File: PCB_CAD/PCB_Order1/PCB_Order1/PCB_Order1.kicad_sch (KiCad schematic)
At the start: 2 parts, among them IC1 TC58BVG1S3HTA00, U1 STM32H7A3ZITx

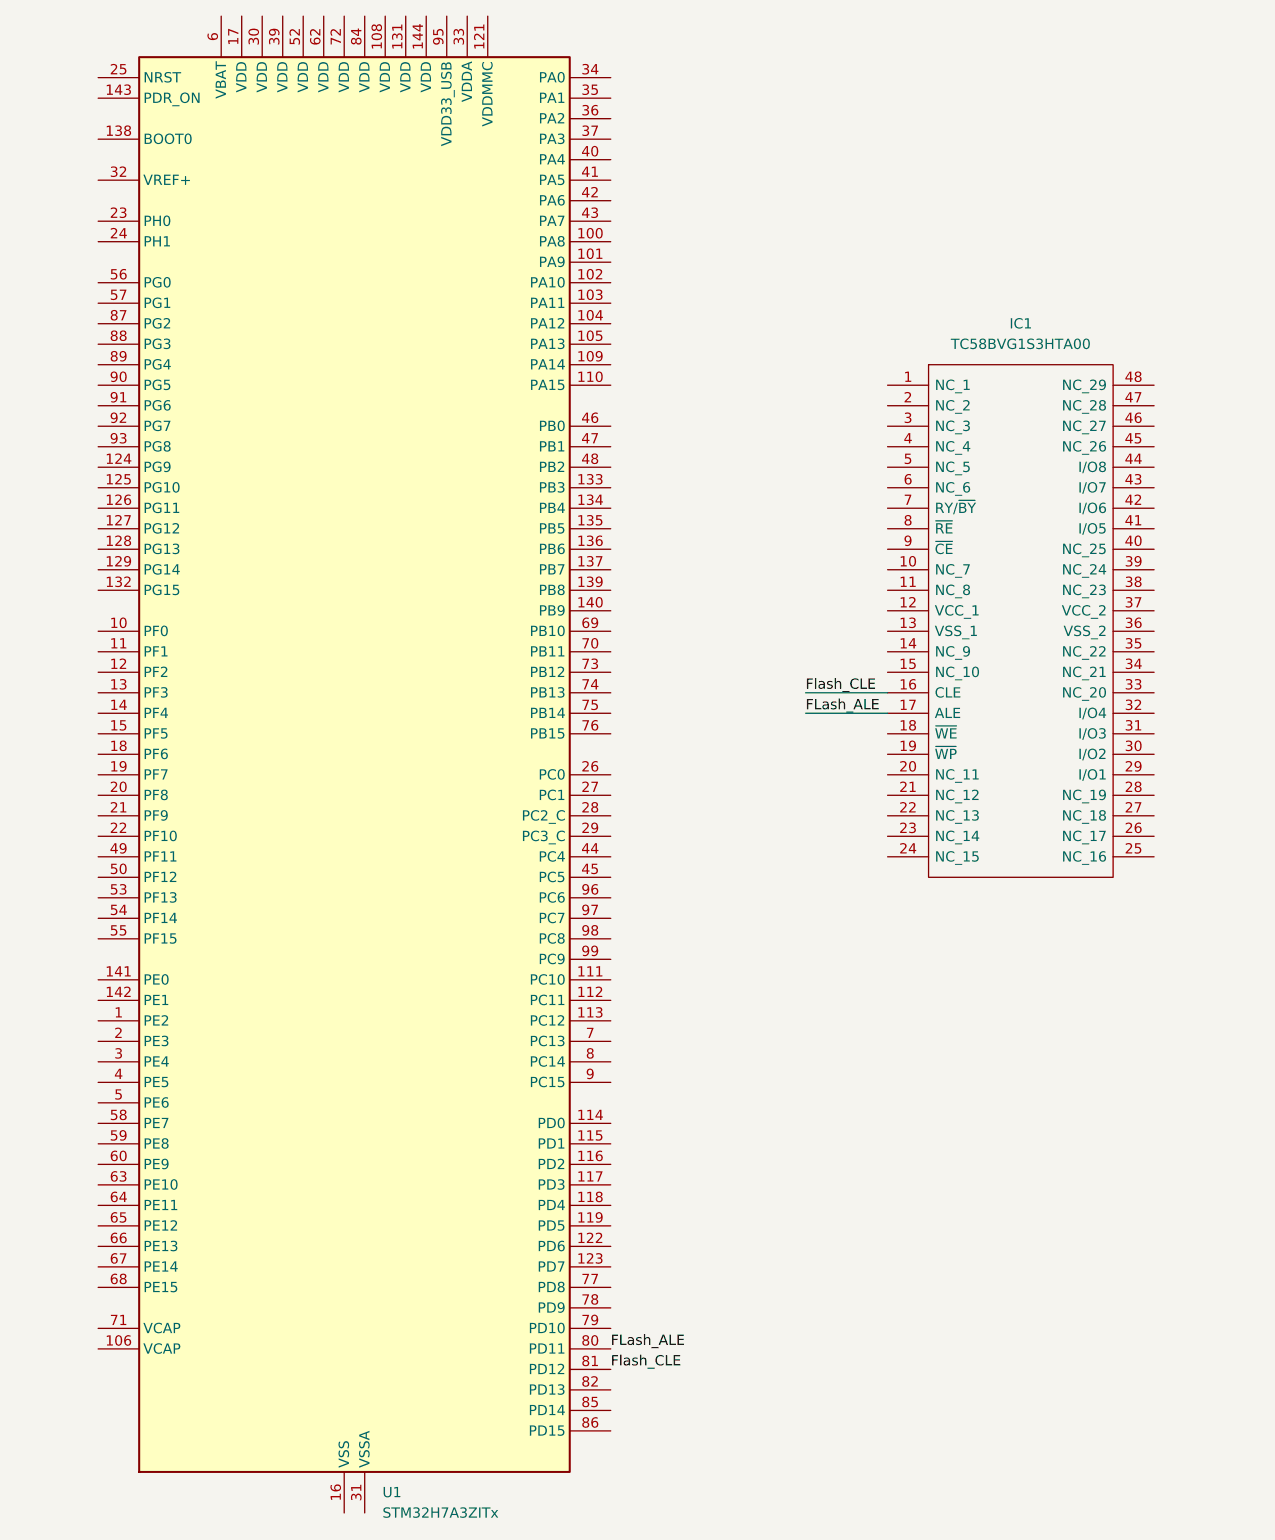
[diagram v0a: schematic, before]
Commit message: Connected all data and logic lines from flash to ucontroller. Power lines still unconnected
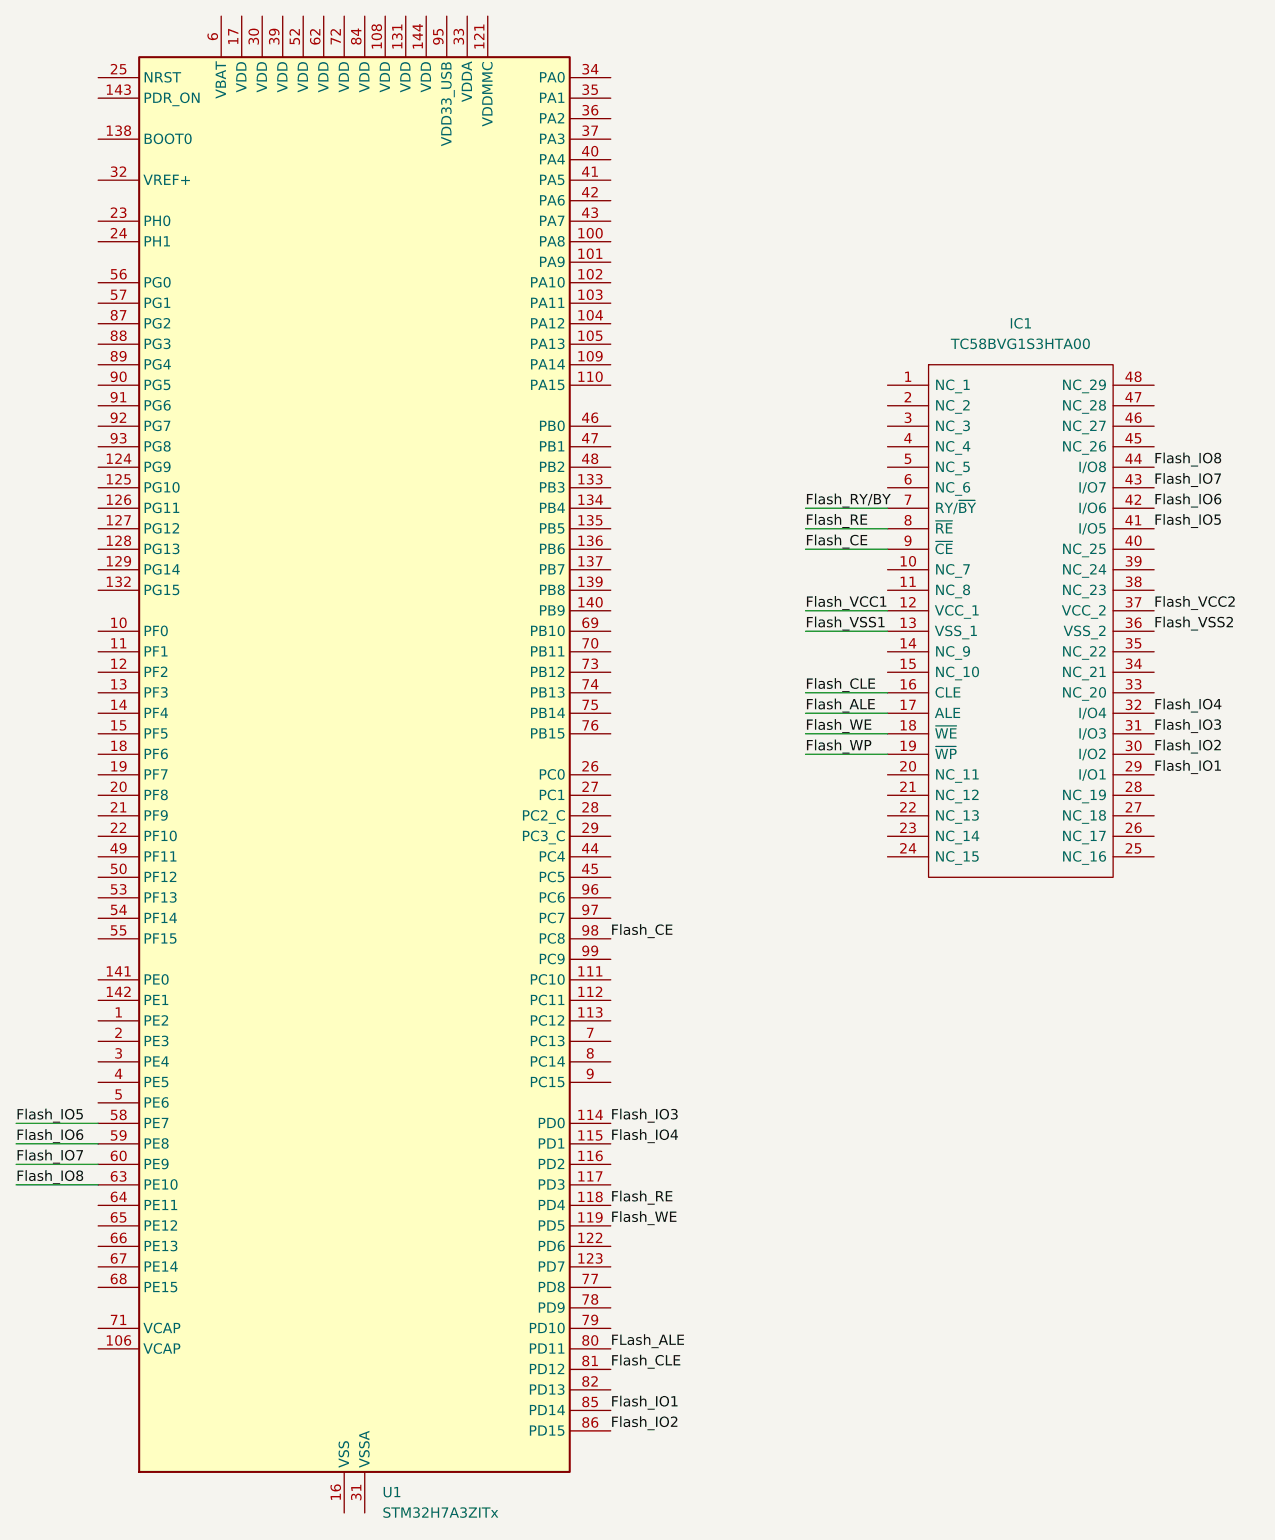
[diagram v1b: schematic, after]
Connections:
- net FLash_ALE: no longer IC1.17 (ALE)
- net Flash_VCC1: now reaches IC1.12 (VCC_1)
- net Flash_VSS1: now reaches IC1.13 (VSS_1)
- net Flash_WE: now reaches IC1.18 (~{WE})
- net Flash_WE: now also U1.119 (PD5)
- net Flash_WP: now reaches IC1.19 (~{WP})
- net Flash_IO1: now reaches IC1.29 (I/O1)
- net Flash_IO1: now also U1.85 (PD14)
- net Flash_IO2: now reaches IC1.30 (I/O2)
- net Flash_IO2: now also U1.86 (PD15)
- net Flash_IO3: now reaches IC1.31 (I/O3)
- net Flash_IO3: now also U1.114 (PD0)
- net Flash_IO4: now reaches IC1.32 (I/O4)
- net Flash_IO4: now also U1.115 (PD1)
- net Flash_VSS2: now reaches IC1.36 (VSS_2)
- net Flash_VCC2: now reaches IC1.37 (VCC_2)
- net Flash_IO5: now reaches IC1.41 (I/O5)
- net Flash_IO5: now also U1.58 (PE7)
- net Flash_IO6: now reaches IC1.42 (I/O6)
- net Flash_IO6: now also U1.59 (PE8)
- net Flash_IO7: now reaches IC1.43 (I/O7)
- net Flash_IO7: now also U1.60 (PE9)
- net Flash_IO8: now reaches IC1.44 (I/O8)
- net Flash_IO8: now also U1.63 (PE10)
- net Flash_RY/BY: now reaches IC1.7 (RY/~{BY})
- net Flash_RE: now reaches IC1.8 (~{RE})
- net Flash_RE: now also U1.118 (PD4)
- net Flash_CE: now reaches IC1.9 (~{CE})
- net Flash_CE: now also U1.98 (PC8)
- new net Flash_ALE: IC1.17 (ALE)
